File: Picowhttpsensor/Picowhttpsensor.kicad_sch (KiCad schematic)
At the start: 1 part

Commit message: add gitignore
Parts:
- removed A1: SC0918, Raspberry Pi:MODULE_SC0918, symbol Raspberry_Pi_Pico_W_SC0918:SC0918
- added J1: Z-ICS0S40P-W000, Z-ICS0S40P-W000:ZICS0S40PW000, symbol Z-ICS0S40P-W000:Z-ICS0S40P-W000
- added U1: Pico, MCU_RaspberryPi_and_Boards:RPi_Pico_SMD_TH, symbol MCU_RaspberryPi_and_Boards:Pico
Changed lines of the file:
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@@
     (title "Picohttpsensor")
   )
-  (symbol (lib_id "Raspberry_Pi_Pico_W_SC0918:SC0918") (at 134.62 105.41 0) (unit 1)
+  (symbol (lib_id "Z-ICS0S40P-W000:Z-ICS0S40P-W000") (at 69.85 66.04 0) (unit 1)
     (in_bom yes) (on_board yes) (dnp no) (fields_autoplaced)
-    (property "Reference" "A1" (at 134.62 52.07 0)
+    (property "Reference" "J1" (at 81.28 58.42 0)
       (effects (font (size 1.27 1.27)))
     )
-    (property "Value" "SC0918" (at 134.62 54.61 0)
+    (property "Value" "Z-ICS0S40P-W000" (at 81.28 60.96 0)
       (effects (font (size 1.27 1.27)))
     )
-    (property "Footprint" "Raspberry Pi:MODULE_SC0918" (at 134.62 57.15 0)
-      (effects (font (size 1.27 1.27)))
+    (property "Footprint" "Z-ICS0S40P-W000:ZICS0S40PW000" (at 88.9 63.5 0)
+      (effects (font (size 1.27 1.27)) (justify left) hide)
     )
-    (property "Datasheet" "https://datasheets.raspberrypi.com/picow/pico-w-datasheet.pdf" (at 107.95 154.94 0)
-      (effects (font (size 1.27 1.27)) (justify left bottom) hide)
+    (property "Datasheet" "https://www.edadoc.com.cn/datasheet/03/4D/J0015383-Z-ICS0S40P-W000.pdf?attname=wKgyIGMNXfGACFRNAANoFyojWLM858.pdf" (at 88.9 66.04 0)
+      (effects (font (size 1.27 1.27)) (justify left) hide)
     )
-    (property "manufacturer" "Raspberry Pi" (at 134.62 59.69 0)
-      (effects (font (size 1.27 1.27)))
+    (property "Description" "DIP Tin 15.24mm 40 2.54mm DIP-40  IC Sockets ROHS" (at 88.9 68.58 0)
+      (effects (font (size 1.27 1.27)) (justify left) hide)
     )
-    (property "P/N" "SC0918" (at 134.62 54.61 0)
-      (effects (font (size 1.27 1.27)) hide)
+    (property "Height" "5.3" (at 88.9 71.12 0)
+      (effects (font (size 1.27 1.27)) (justify left) hide)
     )
-    (property "PARTREV" "1.6" (at 134.62 57.15 0)
-      (effects (font (size 1.27 1.27)) hide)
+    (property "Manufacturer_Name" "Ckmtw(Shenzhen Cankemeng)" (at 88.9 73.66 0)
+      (effects (font (size 1.27 1.27)) (justify left) hide)
     )
-    (property "MAXIMUM_PACKAGE_HEIGHT" "3.73mm" (at 134.62 59.69 0)
-      (effects (font (size 1.27 1.27)) hide)
+    (property "Manufacturer_Part_Number" "Z-ICS0S40P-W000" (at 88.9 76.2 0)
+      (effects (font (size 1.27 1.27)) (justify left) hide)
+    )
+    (property "Mouser Part Number" "" (at 88.9 78.74 0)
+      (effects (font (size 1.27 1.27)) (justify left) hide)
+    )
+    (property "Mouser Price/Stock" "" (at 88.9 81.28 0)
+      (effects (font (size 1.27 1.27)) (justify left) hide)
+    )
+    (property "Arrow Part Number" "" (at 88.9 83.82 0)
+      (effects (font (size 1.27 1.27)) (justify left) hide)
+    )
+    (property "Arrow Price/Stock" "" (at 88.9 86.36 0)
+      (effects (font (size 1.27 1.27)) (justify left) hide)
     )
     (pin "1")
@@
       (project "Picowhttpsensor"
         (path "/0bf090f4-b9b7-437f-9e6a-e818f47752ec"
-          (reference "A1") (unit 1)
+          (reference "J1") (unit 1)
         )
       )
+    )
+  )
+  (symbol (lib_id "MCU_RaspberryPi_and_Boards:Pico") (at 133.35 88.9 0) (unit 1)
+    (in_bom yes) (on_board yes) (dnp no) (fields_autoplaced)
+    (property "Reference" "U1" (at 133.35 57.15 0)
+      (effects (font (size 1.27 1.27)))
+    )
+    (property "Value" "Pico" (at 133.35 59.69 0)
+      (effects (font (size 1.27 1.27)))
+    )
+    (property "Footprint" "MCU_RaspberryPi_and_Boards:RPi_Pico_SMD_TH" (at 133.35 88.9 90)
+      (effects (font (size 1.27 1.27)) hide)
+    )
+    (property "Datasheet" "" (at 133.35 88.9 0)
+      (effects (font (size 1.27 1.27)) hide)
+    )
+    (pin "1")
+    (pin "10")
+    (pin "11")
+    (pin "12")
+    (pin "13")
+    (pin "14")
+    (pin "15")
+    (pin "16")
+    (pin "17")
+    (pin "18")
+    (pin "19")
+    (pin "2")
+    (pin "20")
+    (pin "21")
+    (pin "22")
+    (pin "23")
+    (pin "24")
+    (pin "25")
+    (pin "26")
+    (pin "27")
+    (pin "28")
+    (pin "29")
+    (pin "3")
+    (pin "30")
+    (pin "31")
+    (pin "32")
+    (pin "33")
+    (pin "34")
+    (pin "35")
+    (pin "36")
+    (pin "37")
+    (pin "38")
+    (pin "39")
+    (pin "4")
+    (pin "40")
+    (pin "41")
+    (pin "42")
+    (pin "43")
+    (pin "5")
+    (pin "6")
+    (pin "7")
+    (pin "8")
+    (pin "9")
+    (instances
+      (project "Picowhttpsensor"
+        (path "/0bf090f4-b9b7-437f-9e6a-e818f47752ec"
+          (reference "U1") (unit 1)
+        )
+      )

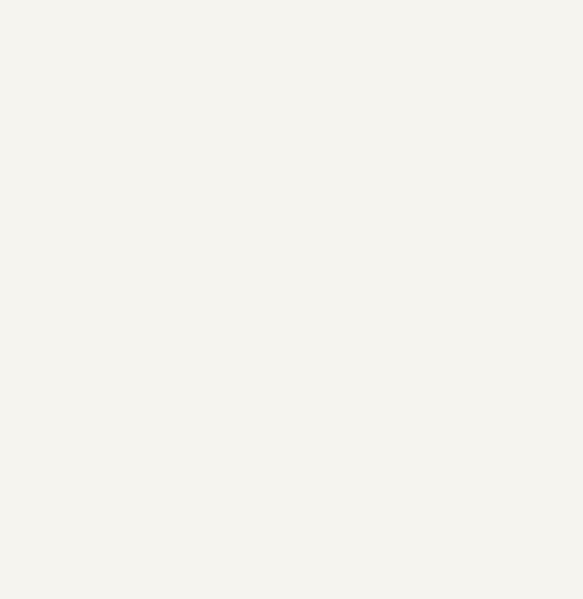
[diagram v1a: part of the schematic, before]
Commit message: add aht20
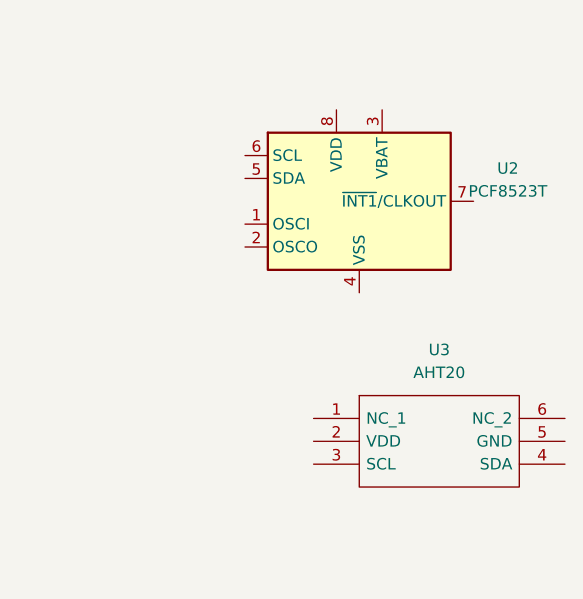
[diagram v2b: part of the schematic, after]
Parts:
- added U2: PCF8523T, Package_SO:SOIC-8_3.9x4.9mm_P1.27mm, symbol Timer_RTC:PCF8523T
- added U3: AHT20, AHT20:AHT20, symbol AHT20:AHT20
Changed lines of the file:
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@@
     (title "Picohttpsensor")
+  )
+  (symbol (lib_id "AHT20:AHT20") (at 220.98 100.33 0) (unit 1)
+    (in_bom yes) (on_board yes) (dnp no) (fields_autoplaced)
+    (property "Reference" "U3" (at 234.95 92.71 0)
+      (effects (font (size 1.27 1.27)))
+    )
+    (property "Value" "AHT20" (at 234.95 95.25 0)
+      (effects (font (size 1.27 1.27)))
+    )
+    (property "Footprint" "AHT20:AHT20" (at 245.11 97.79 0)
+      (effects (font (size 1.27 1.27)) (justify left) hide)
+    )
+    (property "Datasheet" "http://www.aosong.com/userfiles/files/media/Data%20Sheet%20AHT20.pdf" (at 245.11 100.33 0)
+      (effects (font (size 1.27 1.27)) (justify left) hide)
+    )
+    (property "Description" "Integrated temperature and humidity Sensor DC : 2.2 - 5.5V, 0 ~{} 100% RH, -40 ~{} + 85 ." (at 245.11 102.87 0)
+      (effects (font (size 1.27 1.27)) (justify left) hide)
+    )
+    (property "Height" "1.1" (at 245.11 105.41 0)
+      (effects (font (size 1.27 1.27)) (justify left) hide)
+    )
+    (property "Manufacturer_Name" "Aosong" (at 245.11 107.95 0)
+      (effects (font (size 1.27 1.27)) (justify left) hide)
+    )
+    (property "Manufacturer_Part_Number" "AHT20" (at 245.11 110.49 0)
+      (effects (font (size 1.27 1.27)) (justify left) hide)
+    )
+    (property "Mouser Part Number" "" (at 245.11 113.03 0)
+      (effects (font (size 1.27 1.27)) (justify left) hide)
+    )
+    (property "Mouser Price/Stock" "" (at 245.11 115.57 0)
+      (effects (font (size 1.27 1.27)) (justify left) hide)
+    )
+    (property "Arrow Part Number" "" (at 245.11 118.11 0)
+      (effects (font (size 1.27 1.27)) (justify left) hide)
+    )
+    (property "Arrow Price/Stock" "" (at 245.11 120.65 0)
+      (effects (font (size 1.27 1.27)) (justify left) hide)
+    )
+    (pin "1")
+    (pin "2")
+    (pin "3")
+    (pin "4")
+    (pin "5")
+    (pin "6")
+    (instances
+      (project "Picowhttpsensor"
+        (path "/0bf090f4-b9b7-437f-9e6a-e818f47752ec"
+          (reference "U3") (unit 1)
+        )
+      )
+    )
   )
   (symbol (lib_id "Z-ICS0S40P-W000:Z-ICS0S40P-W000") (at 69.85 66.04 0) (unit 1)
@@
         )
       )
+    )
+  )
+  (symbol (lib_id "Timer_RTC:PCF8523T") (at 226.06 76.2 0) (unit 1)
+    (in_bom yes) (on_board yes) (dnp no) (fields_autoplaced)
+    (property "Reference" "U2" (at 242.57 72.5521 0)
+      (effects (font (size 1.27 1.27)))
+    )
+    (property "Value" "PCF8523T" (at 242.57 75.0921 0)
+      (effects (font (size 1.27 1.27)))
+    )
+    (property "Footprint" "Package_SO:SOIC-8_3.9x4.9mm_P1.27mm" (at 246.38 85.09 0)
+      (effects (font (size 1.27 1.27)) hide)
+    )
+    (property "Datasheet" "https://www.nxp.com/docs/en/data-sheet/PCF8523.pdf" (at 226.06 76.2 0)
+      (effects (font (size 1.27 1.27)) hide)
+    )
+    (pin "1")
+    (pin "2")
+    (pin "3")
+    (pin "4")
+    (pin "5")
+    (pin "6")
+    (pin "7")
+    (pin "8")
+    (instances
+      (project "Picowhttpsensor"
+        (path "/0bf090f4-b9b7-437f-9e6a-e818f47752ec"
+          (reference "U2") (unit 1)
+        )
+      )
